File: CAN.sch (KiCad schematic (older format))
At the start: 25 parts, among them P1 CAN_conn, P2 CAN_conn, U3 MCP2551-I-SN, U4 LD1117S50TR_SOT223, U5 LD1117S33TR_SOT223, U6 LP38693MP-ADJ

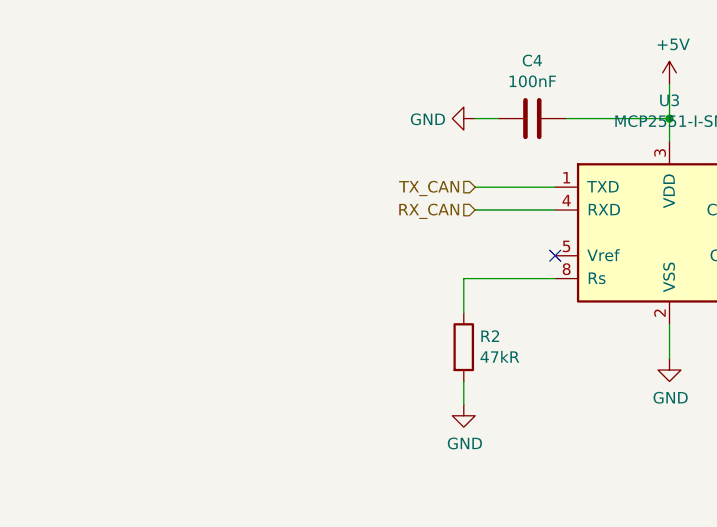
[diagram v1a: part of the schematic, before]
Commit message: PCB routed, no errors but still a few tracks too close
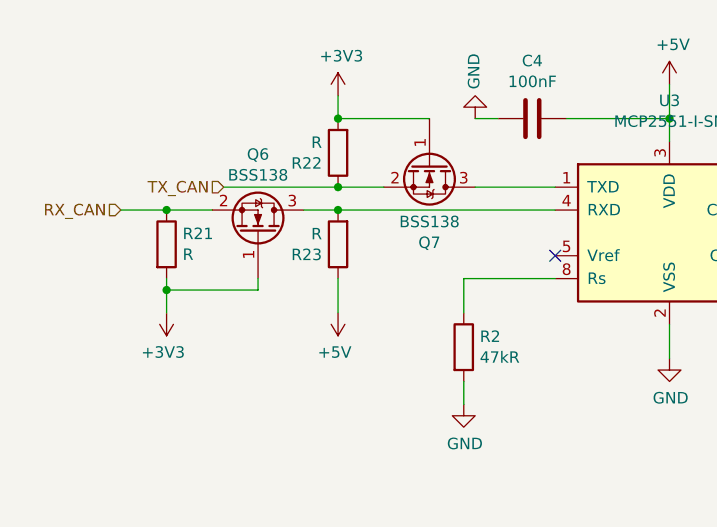
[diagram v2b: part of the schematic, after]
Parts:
- added Q6, Q7: BSS138, Package_TO_SOT_SMD:SOT-23_Handsoldering, symbol Transistor_FET:BSS138
- added R21, R22, R23: R, Resistor_SMD:R_0805_2012Metric_Pad1.15x1.40mm_HandSolder, symbol Device:R
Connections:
- net +3V3: now also Q6.1 (G), Q7.1 (G), R21.2, R22.2
- net +5V: now also R23.1
- net RX_CAN: now also Q6.2 (S), R21.1; no longer U3.4 (RXD)
- net TX_CAN: now also Q7.2 (S), R22.1; no longer U3.1 (TXD)
- new net: Q7.3 (D), U3.1 (TXD)
- new net: Q6.3 (D), R23.2, U3.4 (RXD)
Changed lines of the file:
@@
 Wire Wire Line
 	5250 1400 5250 1550
-Text HLabel 4400 1950 0    50   Input ~ 0
+Text HLabel 2850 1950 0    50   Input ~ 0
 RX_CAN
-Text HLabel 4400 1850 0    50   Input ~ 0
+Text HLabel 3300 1850 0    50   Input ~ 0
 TX_CAN
-Wire Wire Line
-	4400 1850 4750 1850
-Wire Wire Line
-	4400 1950 4750 1950
 $Comp
 L Device:R R2
@@
 F 3 "" H 4400 1550 50  0001 C CNN
 	1    4400 1550
-	0    1    1    0
+	-1   0    0    1
 $EndComp
 Wire Wire Line
@@
 	1    0    0    -1
 $EndComp
+$Comp
+L Transistor_FET:BSS138 Q?
+U 1 1 5BC2AFE8
+P 3450 2050
+AR Path="/5BC2AFE8" Ref="Q?"  Part="1"
+AR Path="/5BBF84F0/5BC2AFE8" Ref="Q?"  Part="1"
+AR Path="/5BBFB7E9/5BC2AFE8" Ref="Q?"  Part="1"
+AR Path="/5BBFB7F2/5BC2AFE8" Ref="Q?"  Part="1"
+AR Path="/5BBFB7F7/5BC2AFE8" Ref="Q?"  Part="1"
+AR Path="/5BBFB807/5BC2AFE8" Ref="Q?"  Part="1"
+AR Path="/5BBFB80C/5BC2AFE8" Ref="Q?"  Part="1"
+AR Path="/5BBFB811/5BC2AFE8" Ref="Q?"  Part="1"
+AR Path="/5BBFB816/5BC2AFE8" Ref="Q?"  Part="1"
+AR Path="/5BBEDBC7/5BC2AFE8" Ref="Q?"  Part="1"
+AR Path="/5BBEFA1A/5BC2AFE8" Ref="Q?"  Part="1"
+AR Path="/5BBEFA89/5BC2AFE8" Ref="Q?"  Part="1"
+AR Path="/5BBA64E1/5BC2AFE8" Ref="Q6"  Part="1"
+F 0 "Q6" V 3793 2050 50  0000 C CNN
+F 1 "BSS138" V 3702 2050 50  0000 C CNN
+F 2 "Package_TO_SOT_SMD:SOT-23_Handsoldering" H 3650 1975 50  0001 L CIN
+F 3 "https://www.fairchildsemi.com/datasheets/BS/BSS138.pdf" H 3450 2050 50  0001 L CNN
+	1    3450 2050
+	0    1    -1   0
+$EndComp
+$Comp
+L Device:R R?
+U 1 1 5BC2AFEF
+P 3050 2100
+AR Path="/5BC2AFEF" Ref="R?"  Part="1"
+AR Path="/5BBF84F0/5BC2AFEF" Ref="R?"  Part="1"
+AR Path="/5BBFB7E9/5BC2AFEF" Ref="R?"  Part="1"
+AR Path="/5BBFB7F2/5BC2AFEF" Ref="R?"  Part="1"
+AR Path="/5BBFB7F7/5BC2AFEF" Ref="R?"  Part="1"
+AR Path="/5BBFB807/5BC2AFEF" Ref="R?"  Part="1"
+AR Path="/5BBFB80C/5BC2AFEF" Ref="R?"  Part="1"
+AR Path="/5BBFB811/5BC2AFEF" Ref="R?"  Part="1"
+AR Path="/5BBFB816/5BC2AFEF" Ref="R?"  Part="1"
+AR Path="/5BBEDBC7/5BC2AFEF" Ref="R?"  Part="1"
+AR Path="/5BBEFA1A/5BC2AFEF" Ref="R?"  Part="1"
+AR Path="/5BBEFA89/5BC2AFEF" Ref="R?"  Part="1"
+AR Path="/5BBA64E1/5BC2AFEF" Ref="R21"  Part="1"
+F 0 "R21" H 3120 2146 50  0000 L CNN
+F 1 "R" H 3120 2055 50  0000 L CNN
+F 2 "Resistor_SMD:R_0805_2012Metric_Pad1.15x1.40mm_HandSolder" V 2980 2100 50  0001 C CNN
+F 3 "~" H 3050 2100 50  0001 C CNN
+	1    3050 2100
+	1    0    0    -1
+$EndComp
+$Comp
+L Device:R R?
+U 1 1 5BC2AFFE
+P 3800 2100
+AR Path="/5BC2AFFE" Ref="R?"  Part="1"
+AR Path="/5BBF84F0/5BC2AFFE" Ref="R?"  Part="1"
+AR Path="/5BBFB7E9/5BC2AFFE" Ref="R?"  Part="1"
+AR Path="/5BBFB7F2/5BC2AFFE" Ref="R?"  Part="1"
+AR Path="/5BBFB7F7/5BC2AFFE" Ref="R?"  Part="1"
+AR Path="/5BBFB807/5BC2AFFE" Ref="R?"  Part="1"
+AR Path="/5BBFB80C/5BC2AFFE" Ref="R?"  Part="1"
+AR Path="/5BBFB811/5BC2AFFE" Ref="R?"  Part="1"
+AR Path="/5BBFB816/5BC2AFFE" Ref="R?"  Part="1"
+AR Path="/5BBEDBC7/5BC2AFFE" Ref="R?"  Part="1"
+AR Path="/5BBEFA1A/5BC2AFFE" Ref="R?"  Part="1"
+AR Path="/5BBEFA89/5BC2AFFE" Ref="R?"  Part="1"
+AR Path="/5BBA64E1/5BC2AFFE" Ref="R23"  Part="1"
+F 0 "R23" H 3870 2146 50  0000 L CNN
+F 1 "R" H 3870 2055 50  0000 L CNN
+F 2 "Resistor_SMD:R_0805_2012Metric_Pad1.15x1.40mm_HandSolder" V 3730 2100 50  0001 C CNN
+F 3 "~" H 3800 2100 50  0001 C CNN
+	1    3800 2100
+	-1   0    0    1
+$EndComp
+Wire Wire Line
+	3800 1950 3650 1950
+$Comp
+L power:+3V3 #PWR?
+U 1 1 5BC2B008
+P 3050 2400
+AR Path="/5BC2B008" Ref="#PWR?"  Part="1"
+AR Path="/5BBF84F0/5BC2B008" Ref="#PWR?"  Part="1"
+AR Path="/5BBFB7E9/5BC2B008" Ref="#PWR?"  Part="1"
+AR Path="/5BBFB7F2/5BC2B008" Ref="#PWR?"  Part="1"
+AR Path="/5BBFB7F7/5BC2B008" Ref="#PWR?"  Part="1"
+AR Path="/5BBFB807/5BC2B008" Ref="#PWR?"  Part="1"
+AR Path="/5BBFB80C/5BC2B008" Ref="#PWR?"  Part="1"
+AR Path="/5BBFB811/5BC2B008" Ref="#PWR?"  Part="1"
+AR Path="/5BBFB816/5BC2B008" Ref="#PWR?"  Part="1"
+AR Path="/5BBEDBC7/5BC2B008" Ref="#PWR?"  Part="1"
+AR Path="/5BBEFA1A/5BC2B008" Ref="#PWR?"  Part="1"
+AR Path="/5BBEFA89/5BC2B008" Ref="#PWR?"  Part="1"
+AR Path="/5BBA64E1/5BC2B008" Ref="#PWR073"  Part="1"
+F 0 "#PWR073" H 3050 2250 50  0001 C CNN
+F 1 "+3V3" H 3065 2573 50  0000 C CNN
+F 2 "" H 3050 2400 50  0001 C CNN
+F 3 "" H 3050 2400 50  0001 C CNN
+	1    3050 2400
+	-1   0    0    1
+$EndComp
+Connection ~ 3800 1950
+$Comp
+L power:+5V #PWR075
+U 1 1 5BC3B053
+P 3800 2400
+F 0 "#PWR075" H 3800 2250 50  0001 C CNN
+F 1 "+5V" H 3815 2573 50  0000 C CNN
+F 2 "" H 3800 2400 50  0001 C CNN
+F 3 "" H 3800 2400 50  0001 C CNN
+	1    3800 2400
+	-1   0    0    1
+$EndComp
+Wire Wire Line
+	2850 1950 3050 1950
+Connection ~ 3050 1950
+Wire Wire Line
+	3050 1950 3250 1950
+Wire Wire Line
+	3050 2250 3050 2300
+Wire Wire Line
+	3050 2300 3450 2300
+Wire Wire Line
+	3450 2300 3450 2250
+Connection ~ 3050 2300
+Wire Wire Line
+	3050 2300 3050 2400
+Wire Wire Line
+	3800 2250 3800 2400
+$Comp
+L Transistor_FET:BSS138 Q?
+U 1 1 5BC4D8C0
+P 4200 1750
+AR Path="/5BC4D8C0" Ref="Q?"  Part="1"
+AR Path="/5BBF84F0/5BC4D8C0" Ref="Q?"  Part="1"
+AR Path="/5BBFB7E9/5BC4D8C0" Ref="Q?"  Part="1"
+AR Path="/5BBFB7F2/5BC4D8C0" Ref="Q?"  Part="1"
+AR Path="/5BBFB7F7/5BC4D8C0" Ref="Q?"  Part="1"
+AR Path="/5BBFB807/5BC4D8C0" Ref="Q?"  Part="1"
+AR Path="/5BBFB80C/5BC4D8C0" Ref="Q?"  Part="1"
+AR Path="/5BBFB811/5BC4D8C0" Ref="Q?"  Part="1"
+AR Path="/5BBFB816/5BC4D8C0" Ref="Q?"  Part="1"
+AR Path="/5BBEDBC7/5BC4D8C0" Ref="Q?"  Part="1"
+AR Path="/5BBEFA1A/5BC4D8C0" Ref="Q?"  Part="1"
+AR Path="/5BBEFA89/5BC4D8C0" Ref="Q?"  Part="1"
+AR Path="/5BBA64E1/5BC4D8C0" Ref="Q7"  Part="1"
+F 0 "Q7" V 4543 1750 50  0000 C CNN
+F 1 "BSS138" V 4452 1750 50  0000 C CNN
+F 2 "Package_TO_SOT_SMD:SOT-23_Handsoldering" H 4400 1675 50  0001 L CIN
+F 3 "https://www.fairchildsemi.com/datasheets/BS/BSS138.pdf" H 4200 1750 50  0001 L CNN
+	1    4200 1750
+	0    1    1    0
+$EndComp
+$Comp
+L Device:R R?
+U 1 1 5BC4D8C7
+P 3800 1700
+AR Path="/5BC4D8C7" Ref="R?"  Part="1"
+AR Path="/5BBF84F0/5BC4D8C7" Ref="R?"  Part="1"
+AR Path="/5BBFB7E9/5BC4D8C7" Ref="R?"  Part="1"
+AR Path="/5BBFB7F2/5BC4D8C7" Ref="R?"  Part="1"
+AR Path="/5BBFB7F7/5BC4D8C7" Ref="R?"  Part="1"
+AR Path="/5BBFB807/5BC4D8C7" Ref="R?"  Part="1"
+AR Path="/5BBFB80C/5BC4D8C7" Ref="R?"  Part="1"
+AR Path="/5BBFB811/5BC4D8C7" Ref="R?"  Part="1"
+AR Path="/5BBFB816/5BC4D8C7" Ref="R?"  Part="1"
+AR Path="/5BBEDBC7/5BC4D8C7" Ref="R?"  Part="1"
+AR Path="/5BBEFA1A/5BC4D8C7" Ref="R?"  Part="1"
+AR Path="/5BBEFA89/5BC4D8C7" Ref="R?"  Part="1"
+AR Path="/5BBA64E1/5BC4D8C7" Ref="R22"  Part="1"
+F 0 "R22" H 3870 1746 50  0000 L CNN
+F 1 "R" H 3870 1655 50  0000 L CNN
+F 2 "Resistor_SMD:R_0805_2012Metric_Pad1.15x1.40mm_HandSolder" V 3730 1700 50  0001 C CNN
+F 3 "~" H 3800 1700 50  0001 C CNN
+	1    3800 1700
+	-1   0    0    1
+$EndComp
+Wire Wire Line
+	4000 1850 3800 1850
+Wire Wire Line
+	4200 1550 3800 1550
+Wire Wire Line
+	3800 1550 3800 1450
+Connection ~ 3800 1550
+$Comp
+L power:+3V3 #PWR?
+U 1 1 5BC4D8E0
+P 3800 1450
+AR Path="/5BC4D8E0" Ref="#PWR?"  Part="1"
+AR Path="/5BBF84F0/5BC4D8E0" Ref="#PWR?"  Part="1"
+AR Path="/5BBFB7E9/5BC4D8E0" Ref="#PWR?"  Part="1"
+AR Path="/5BBFB7F2/5BC4D8E0" Ref="#PWR?"  Part="1"
+AR Path="/5BBFB7F7/5BC4D8E0" Ref="#PWR?"  Part="1"
+AR Path="/5BBFB807/5BC4D8E0" Ref="#PWR?"  Part="1"
+AR Path="/5BBFB80C/5BC4D8E0" Ref="#PWR?"  Part="1"
+AR Path="/5BBFB811/5BC4D8E0" Ref="#PWR?"  Part="1"
+AR Path="/5BBFB816/5BC4D8E0" Ref="#PWR?"  Part="1"
+AR Path="/5BBEDBC7/5BC4D8E0" Ref="#PWR?"  Part="1"
+AR Path="/5BBEFA1A/5BC4D8E0" Ref="#PWR?"  Part="1"
+AR Path="/5BBEFA89/5BC4D8E0" Ref="#PWR?"  Part="1"
+AR Path="/5BBA64E1/5BC4D8E0" Ref="#PWR074"  Part="1"
+F 0 "#PWR074" H 3800 1300 50  0001 C CNN
+F 1 "+3V3" H 3815 1623 50  0000 C CNN
+F 2 "" H 3800 1450 50  0001 C CNN
+F 3 "" H 3800 1450 50  0001 C CNN
+	1    3800 1450
+	1    0    0    -1
+$EndComp
+Wire Wire Line
+	3800 1850 3300 1850
+Connection ~ 3800 1850
+Wire Wire Line
+	4400 1850 4750 1850
+Wire Wire Line
+	3800 1950 4750 1950
 $EndSCHEMATC

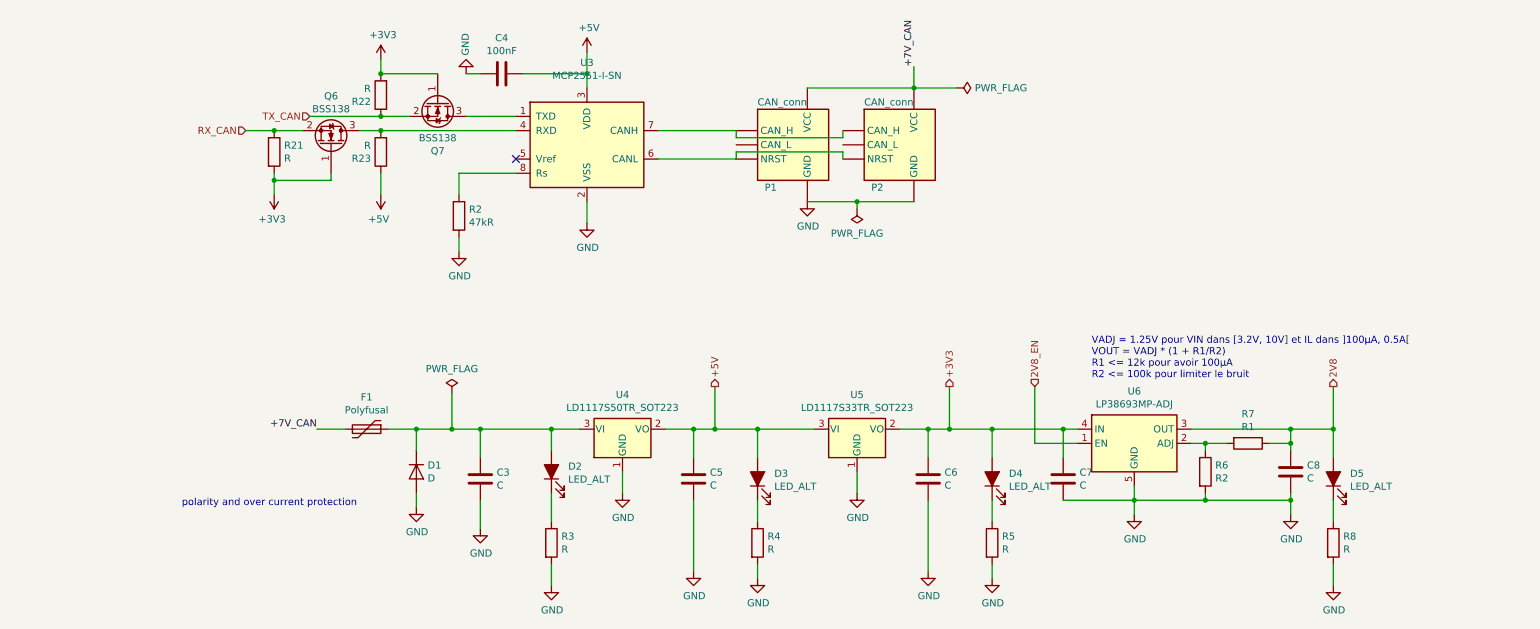
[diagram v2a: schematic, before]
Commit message: Corrected, routing redone
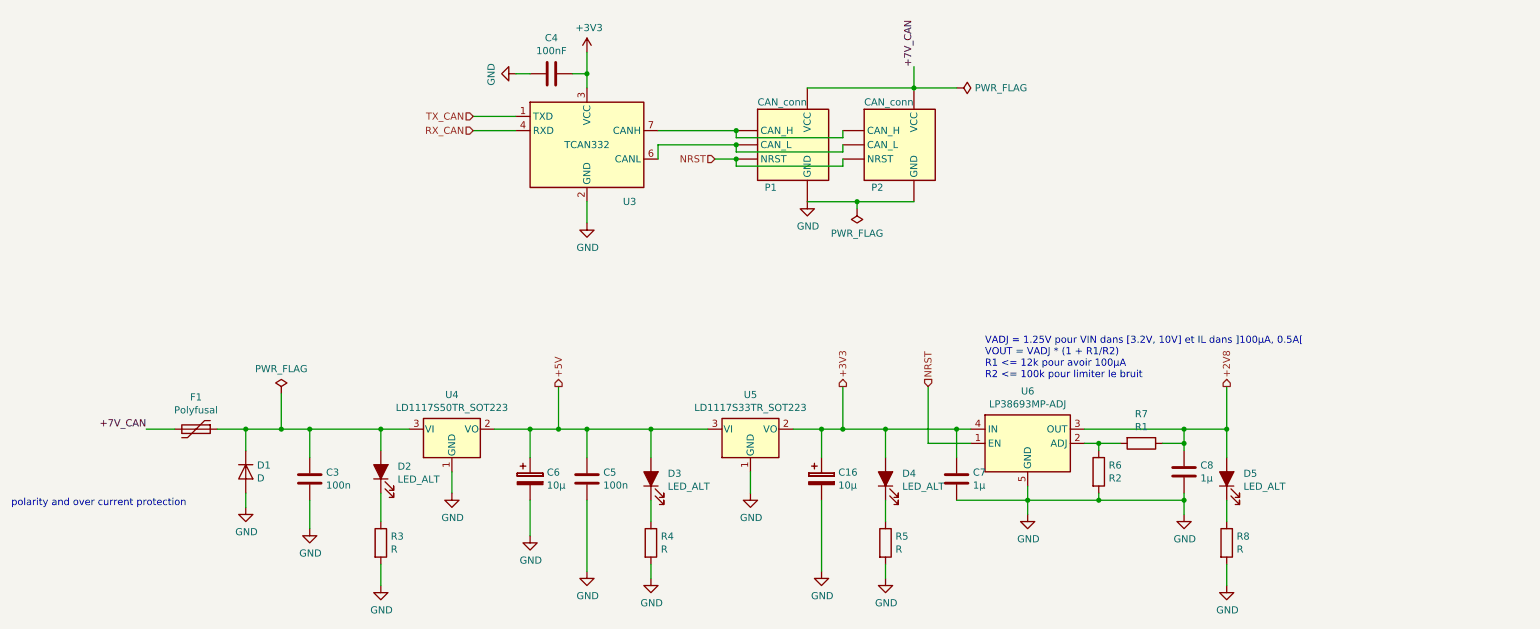
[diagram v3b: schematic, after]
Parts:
- removed C6: C, Capacitor_SMD:C_0805_2012Metric_Pad1.15x1.40mm_HandSolder, symbol Device:C
- removed Q6, Q7: BSS138, Package_TO_SOT_SMD:SOT-23_Handsoldering, symbol Transistor_FET:BSS138
- removed R2: 47kR, Resistor_SMD:R_0805_2012Metric_Pad1.15x1.40mm_HandSolder, symbol Device:R
- removed R21, R22, R23: R, Resistor_SMD:R_0805_2012Metric_Pad1.15x1.40mm_HandSolder, symbol Device:R
- removed U3: MCP2551-I-SN, Package_SO:SOIC-8_3.9x4.9mm_P1.27mm, symbol Interface_CAN_LIN:MCP2551-I-SN
- added C16, C6: 10µ, Capacitor_SMD:CP_Elec_4x5.4, symbol Device:CP
- added U3: TCAN332, Package_SO:SOIC-8_3.9x4.9mm_P1.27mm, symbol Interface_CAN_LIN:TCAN332
- C3, C5: value C -> 100n
- C7, C8: value C -> 1µ
- P1, P2: footprint Connector_JST:JST_XH_B04B-XH-A_1x04_P2.50mm_Vertical -> Connector_JST:JST_XH_B05B-XH-A_1x05_P2.50mm_Vertical
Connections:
- net 2V8_EN is gone; now on net NRST: U6.1 (EN)
- net +3V3: now also C4.1, C16.1, U3.3 (VCC)
- net +5V: now also C6.1; no longer C4.1
- net GND: now also C16.2, C6.2, U3.2 (GND)
- net RX_CAN: now also U3.4 (RXD)
- net TX_CAN: now also U3.1 (TXD)
- net NRST: now reaches P1.2 (NRST), P2.2 (NRST)
- net at P1.3 (CAN_L): now also P2.3 (CAN_L), U3.6 (CANL)
- net at P1.4 (CAN_H), P2.4 (CAN_H): now also U3.7 (CANH)
- net 2V8 renamed +2V8
- no-connect marks 1 -> 0
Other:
- moved on the sheet: C3, C4, C5, C7, C8, D1, D2, D3, D4, D5, F1, R3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

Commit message: Added RS refs
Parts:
- C16, C6: RS (none) -> 708-5815
- C7, C8: RS (none) -> 133-5653
- D2, D3, D4, D5: RS (none) -> 174-9844,174-9849
- P1, P2: RS (none) -> 820-1560
- U3: RS (none) -> 133-0714
- U4: RS (none) -> 686-9379
- U5: RS (none) -> 714-0697
- U6: RS (none) -> 537-9222
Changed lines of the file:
@@
 F 2 "Connector_JST:JST_XH_B05B-XH-A_1x05_P2.50mm_Vertical" H 6850 1700 50  0001 C CNN
 F 3 "https://github.com/PhenixRobotik/phenix_kicad" H 7149 1959 50  0001 L CNN
+F 4 "820-1560" H 0   0   50  0001 C CNN "RS"
 	1    6700 2050
 	1    0    0    -1
@@
 F 2 "Connector_JST:JST_XH_B05B-XH-A_1x05_P2.50mm_Vertical" H 7600 1700 50  0001 C CNN
 F 3 "https://github.com/PhenixRobotik/phenix_kicad" H 7899 1959 50  0001 L CNN
+F 4 "820-1560" H 0   0   50  0001 C CNN "RS"
 	1    7450 2050
 	1    0    0    -1
@@
 F 2 "Package_TO_SOT_SMD:SOT-223-3_TabPin2" H 6400 4250 50  0001 C CNN
 F 3 "http://www.st.com/st-web-ui/static/active/en/resource/technical/document/datasheet/CD00000544.pdf" H 6500 3800 50  0001 C CNN
+F 4 "714-0697" H 0   0   50  0001 C CNN "RS"
 	1    6400 4050
 	1    0    0    -1
@@
 F 2 "LED_SMD:LED_0805_2012Metric_Castellated" H 7350 4400 50  0001 C CNN
 F 3 "~" H 7350 4400 50  0001 C CNN
+F 4 "174-9844,174-9849" H 0   0   50  0001 C CNN "RS"
 	1    7350 4400
 	0    -1   -1   0
@@
 F 2 "LED_SMD:LED_0805_2012Metric_Castellated" H 9750 4400 50  0001 C CNN
 F 3 "~" H 9750 4400 50  0001 C CNN
+F 4 "174-9844,174-9849" H 0   0   50  0001 C CNN "RS"
 	1    9750 4400
 	0    -1   -1   0
@@
 F 2 "LED_SMD:LED_0805_2012Metric_Castellated" H 3800 4350 50  0001 C CNN
 F 3 "~" H 3800 4350 50  0001 C CNN
+F 4 "174-9844,174-9849" H 0   0   50  0001 C CNN "RS"
 	1    3800 4350
 	0    -1   -1   0
@@
 F 2 "Capacitor_SMD:C_0805_2012Metric_Pad1.15x1.40mm_HandSolder" H 7888 4250 50  0001 C CNN
 F 3 "~" H 7850 4400 50  0001 C CNN
+F 4 "133-5653" H 0   0   50  0001 C CNN "RS"
 	1    7850 4400
 	-1   0    0    1
@@
 F 2 "Capacitor_SMD:C_0805_2012Metric_Pad1.15x1.40mm_HandSolder" H 9488 4200 50  0001 C CNN
 F 3 "~" H 9450 4350 50  0001 C CNN
+F 4 "133-5653" H 0   0   50  0001 C CNN "RS"
 	1    9450 4350
 	1    0    0    -1
@@
 F 2 "LED_SMD:LED_0805_2012Metric_Castellated" H 5700 4400 50  0001 C CNN
 F 3 "~" H 5700 4400 50  0001 C CNN
+F 4 "174-9844,174-9849" H 0   0   50  0001 C CNN "RS"
 	1    5700 4400
 	0    -1   -1   0
@@
 F 2 "Package_TO_SOT_SMD:SOT-223-3_TabPin2" H 4300 4250 50  0001 C CNN
 F 3 "http://www.st.com/st-web-ui/static/active/en/resource/technical/document/datasheet/CD00000544.pdf" H 4400 3800 50  0001 C CNN
+F 4 "686-9379" H 0   0   50  0001 C CNN "RS"
 	1    4300 4050
 	1    0    0    -1
@@
 F 2 "Package_TO_SOT_SMD:SOT-223-5" H 8350 3900 50  0001 C CNN
 F 3 "http://www.ti.com/lit/ds/snvs324k/snvs324k.pdf" H 8350 4150 50  0001 C CNN
+F 4 "537-9222" H 0   0   50  0001 C CNN "RS"
 	1    8350 4150
 	1    0    0    -1
@@
 F 2 "Capacitor_SMD:CP_Elec_4x5.4" H 4888 4250 50  0001 C CNN
 F 3 "~" H 4850 4400 50  0001 C CNN
+F 4 " 708-5815" H 0   0   50  0001 C CNN "RS"
 	1    4850 4400
 	1    0    0    -1
@@
 F 2 "Capacitor_SMD:CP_Elec_4x5.4" H 6938 4250 50  0001 C CNN
 F 3 "~" H 6900 4400 50  0001 C CNN
+F 4 " 708-5815" H 0   0   50  0001 C CNN "RS"
 	1    6900 4400
 	1    0    0    -1
@@
 F 2 "Package_SO:SOIC-8_3.9x4.9mm_P1.27mm" H 5250 1550 50  0001 C CIN
 F 3 "http://www.ti.com/lit/ds/symlink/tcan337.pdf" H 5250 2050 50  0001 C CNN
+F 4 "133-0714" H 0   0   50  0001 C CNN "RS"
 	1    5250 2050
 	1    0    0    -1
@@
 NRST
 $Comp
-L power:+3V3 #PWR?
+L power:+3V3 #PWR0101
 U 1 1 5BD33885
 P 5250 1400
-F 0 "#PWR?" H 5250 1250 50  0001 C CNN
+F 0 "#PWR0101" H 5250 1250 50  0001 C CNN
 F 1 "+3V3" H 5265 1573 50  0000 C CNN
 F 2 "" H 5250 1400 50  0001 C CNN

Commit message: Improved text placement
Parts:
- P1, P2: symbol PhoenixRobotik:CAN_conn -> PhenixRobotik:CAN_conn
- U6: symbol PhoenixRobotik:LP38693MP-ADJ -> PhenixRobotik:LP38693MP-ADJ
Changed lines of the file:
@@
 $EndDescr
 $Comp
-L PhoenixRobotik:CAN_conn P1
+L PhenixRobotik:CAN_conn P1
 U 1 1 5B231012
 P 6700 2050
@@
 TX_CAN
 $Comp
-L PhoenixRobotik:CAN_conn P2
+L PhenixRobotik:CAN_conn P2
 U 1 1 5BADEF26
 P 7450 2050
@@
 	7550 1650 7850 1650
 $Comp
-L PhoenixRobotik:LP38693MP-ADJ U6
+L PhenixRobotik:LP38693MP-ADJ U6
 U 1 1 5BC2B40F
 P 8350 4150

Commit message: Added component values
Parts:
- C4: value 100nF -> 100n
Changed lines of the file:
@@
 EESchema Schematic File Version 4
-LIBS:ultraphotonicsense-elec-cache
 EELAYER 26 0
 EELAYER END
@@
 P 5000 1550
 F 0 "C4" V 4748 1550 50  0000 C CNN
-F 1 "100nF" V 4839 1550 50  0000 C CNN
+F 1 "100n" V 4839 1550 50  0000 C CNN
 F 2 "Capacitor_SMD:C_0805_2012Metric_Pad1.15x1.40mm_HandSolder" H 5038 1400 50  0001 C CNN
 F 3 "~" H 5000 1550 50  0001 C CNN

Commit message: Added resistors values
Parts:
- R3: value R -> 700
- R4: value R -> 500
- R5: value R -> 330
- R6: value R2 -> 6.8k
- R7: value R1 -> 9.1k
- R8: value R -> 280
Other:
- note added: "R7 = 1.24*R6"
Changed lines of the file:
@@
 AR Path="/5BBA64E1/5BAEB68C" Ref="R5"  Part="1"
 F 0 "R5" H 7420 4896 50  0000 L CNN
-F 1 "R" H 7420 4805 50  0000 L CNN
+F 1 "330" H 7420 4805 50  0000 L CNN
 F 2 "Resistor_SMD:R_0805_2012Metric_Pad1.15x1.40mm_HandSolder" V 7280 4850 50  0001 C CNN
 F 3 "~" H 7350 4850 50  0001 C CNN
@@
 AR Path="/5BBA64E1/5BAEB693" Ref="R8"  Part="1"
 F 0 "R8" H 9820 4896 50  0000 L CNN
-F 1 "R" H 9820 4805 50  0000 L CNN
+F 1 "280" H 9820 4805 50  0000 L CNN
 F 2 "Resistor_SMD:R_0805_2012Metric_Pad1.15x1.40mm_HandSolder" V 9680 4850 50  0001 C CNN
 F 3 "~" H 9750 4850 50  0001 C CNN
@@
 AR Path="/5BBA64E1/5BAEB705" Ref="R3"  Part="1"
 F 0 "R3" H 3870 4896 50  0000 L CNN
-F 1 "R" H 3870 4805 50  0000 L CNN
+F 1 "700" H 3870 4805 50  0000 L CNN
 F 2 "Resistor_SMD:R_0805_2012Metric_Pad1.15x1.40mm_HandSolder" V 3730 4850 50  0001 C CNN
 F 3 "~" H 3800 4850 50  0001 C CNN
@@
 P 8850 4350
 F 0 "R6" H 8920 4396 50  0000 L CNN
-F 1 "R2" H 8920 4305 50  0000 L CNN
+F 1 "6.8k" H 8920 4305 50  0000 L CNN
 F 2 "Resistor_SMD:R_0805_2012Metric_Pad1.15x1.40mm_HandSolder" V 8780 4350 50  0001 C CNN
 F 3 "~" H 8850 4350 50  0001 C CNN
@@
 P 9150 4150
 F 0 "R7" V 8943 4150 50  0000 C CNN
-F 1 "R1" V 9034 4150 50  0000 C CNN
+F 1 "9.1k" V 9034 4150 50  0000 C CNN
 F 2 "Resistor_SMD:R_0805_2012Metric_Pad1.15x1.40mm_HandSolder" V 9080 4150 50  0001 C CNN
 F 3 "~" H 9150 4150 50  0001 C CNN
@@
 AR Path="/5BBA64E1/5BBE78C2" Ref="R4"  Part="1"
 F 0 "R4" H 5770 4896 50  0000 L CNN
-F 1 "R" H 5770 4805 50  0000 L CNN
+F 1 "500" H 5770 4805 50  0000 L CNN
 F 2 "Resistor_SMD:R_0805_2012Metric_Pad1.15x1.40mm_HandSolder" V 5630 4850 50  0001 C CNN
 F 3 "~" H 5700 4850 50  0001 C CNN
@@
 	1    0    0    -1
 $EndComp
+Text Notes 8600 4750 0    50   ~ 0
+R7 = 1.24*R6
 $EndSCHEMATC
